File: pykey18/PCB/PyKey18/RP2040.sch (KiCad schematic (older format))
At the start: 37 parts, among them J1 USB_C_Receptacle_USB2.0, J2 Conn_01x03, J3 Conn_01x04, J4 AudioJack4, J5 Conn_01x04, SW101 SW_SPST, SW2 SW_SPDT, U101 RP2040, U102 W25Q128JVS, U103 AMS1117-3.3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

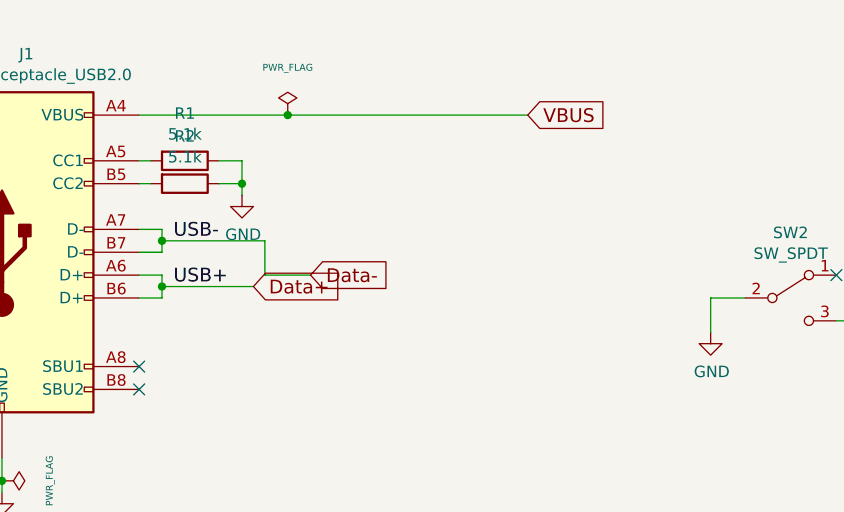
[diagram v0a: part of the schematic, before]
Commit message: add esd protection
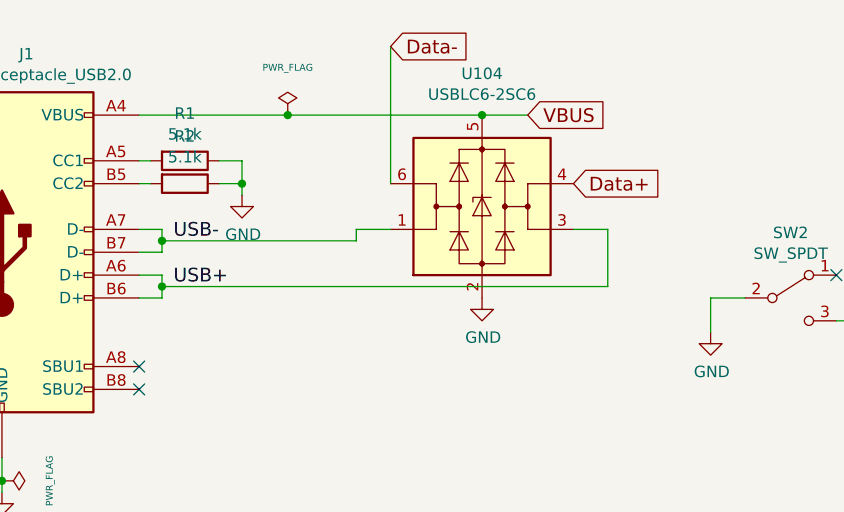
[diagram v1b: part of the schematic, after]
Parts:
- added U104: USBLC6-2SC6, Package_TO_SOT_SMD:SOT-23-6, symbol Power_Protection:USBLC6-2SC6
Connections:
- net Data+: now also U104.4 (I/O2); no longer J1.A6 (D+), J1.B6 (D+)
- net Data-: now also U104.6 (I/O1); no longer J1.A7 (D-), J1.B7 (D-)
- net GND: now also U104.2 (GND)
- net VBUS: now also U104.5 (VBUS)
- new net USB+: J1.A6 (D+), J1.B6 (D+), U104.3 (I/O2)
- new net USB-: J1.A7 (D-), J1.B7 (D-), U104.1 (I/O1)
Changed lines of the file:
@@
 Wire Wire Line
 	5000 2350 4900 2350
-Wire Wire Line
-	5000 2300 5400 2300
 Connection ~ 5000 2300
 Wire Wire Line
@@
 Wire Wire Line
 	5000 2050 5000 2100
-Wire Wire Line
-	5650 2250 5450 2250
-Wire Wire Line
-	5450 2250 5450 2100
-Wire Wire Line
-	5450 2100 5000 2100
 Connection ~ 5000 2100
 Wire Wire Line
 	5000 2100 5000 2150
-Text GLabel 5400 2300 2    60   Input ~ 0
+Text GLabel 6800 1850 2    60   Input ~ 0
 Data+
-Text GLabel 5650 2250 2    60   Input ~ 0
+Text GLabel 6000 1250 2    60   Input ~ 0
 Data-
 Text GLabel 6600 1550 2    60   Input ~ 0
@@
 	4300 3150 4300 3200
 Wire Wire Line
-	5550 1550 6600 1550
+	5550 1550 6400 1550
 Text GLabel 14250 5100 2    60   Input ~ 0
 COL16
@@
 Text GLabel 17600 6650 0    60   Input ~ 0
 I2C1_SCL
+$Comp
+L Power_Protection:USBLC6-2SC6 U104
+U 1 1 619EC863
+P 6400 1950
+F 0 "U104" H 6400 2531 50  0000 C CNN
+F 1 "USBLC6-2SC6" H 6400 2440 50  0000 C CNN
+F 2 "Package_TO_SOT_SMD:SOT-23-6" H 6400 1450 50  0001 C CNN
+F 3 "https://www.st.com/resource/en/datasheet/usblc6-2.pdf" H 6600 2300 50  0001 C CNN
+	1    6400 1950
+	1    0    0    -1
+$EndComp
+Connection ~ 6400 1550
+Wire Wire Line
+	6400 1550 6600 1550
+$Comp
+L power:GND #PWR030
+U 1 1 619F0415
+P 6400 2350
+F 0 "#PWR030" H 6400 2100 50  0001 C CNN
+F 1 "GND" H 6405 2177 50  0000 C CNN
+F 2 "" H 6400 2350 50  0001 C CNN
+F 3 "" H 6400 2350 50  0001 C CNN
+	1    6400 2350
+	1    0    0    -1
+$EndComp
+Wire Wire Line
+	6800 2050 6950 2050
+Wire Wire Line
+	6950 2050 6950 2300
+Wire Wire Line
+	5000 2300 6950 2300
+Wire Wire Line
+	5850 2100 5850 2050
+Wire Wire Line
+	5850 2050 6000 2050
+Wire Wire Line
+	5000 2100 5850 2100
+Wire Wire Line
+	6000 1250 6000 1850
 $EndSCHEMATC
